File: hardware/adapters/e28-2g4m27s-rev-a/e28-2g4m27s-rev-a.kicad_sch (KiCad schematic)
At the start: 18 parts, among them J1 TSW-110-07-G-S, J2 TSW-108-07-G-S, U1 E28-2G4M27S, U2 AP63203WU-7

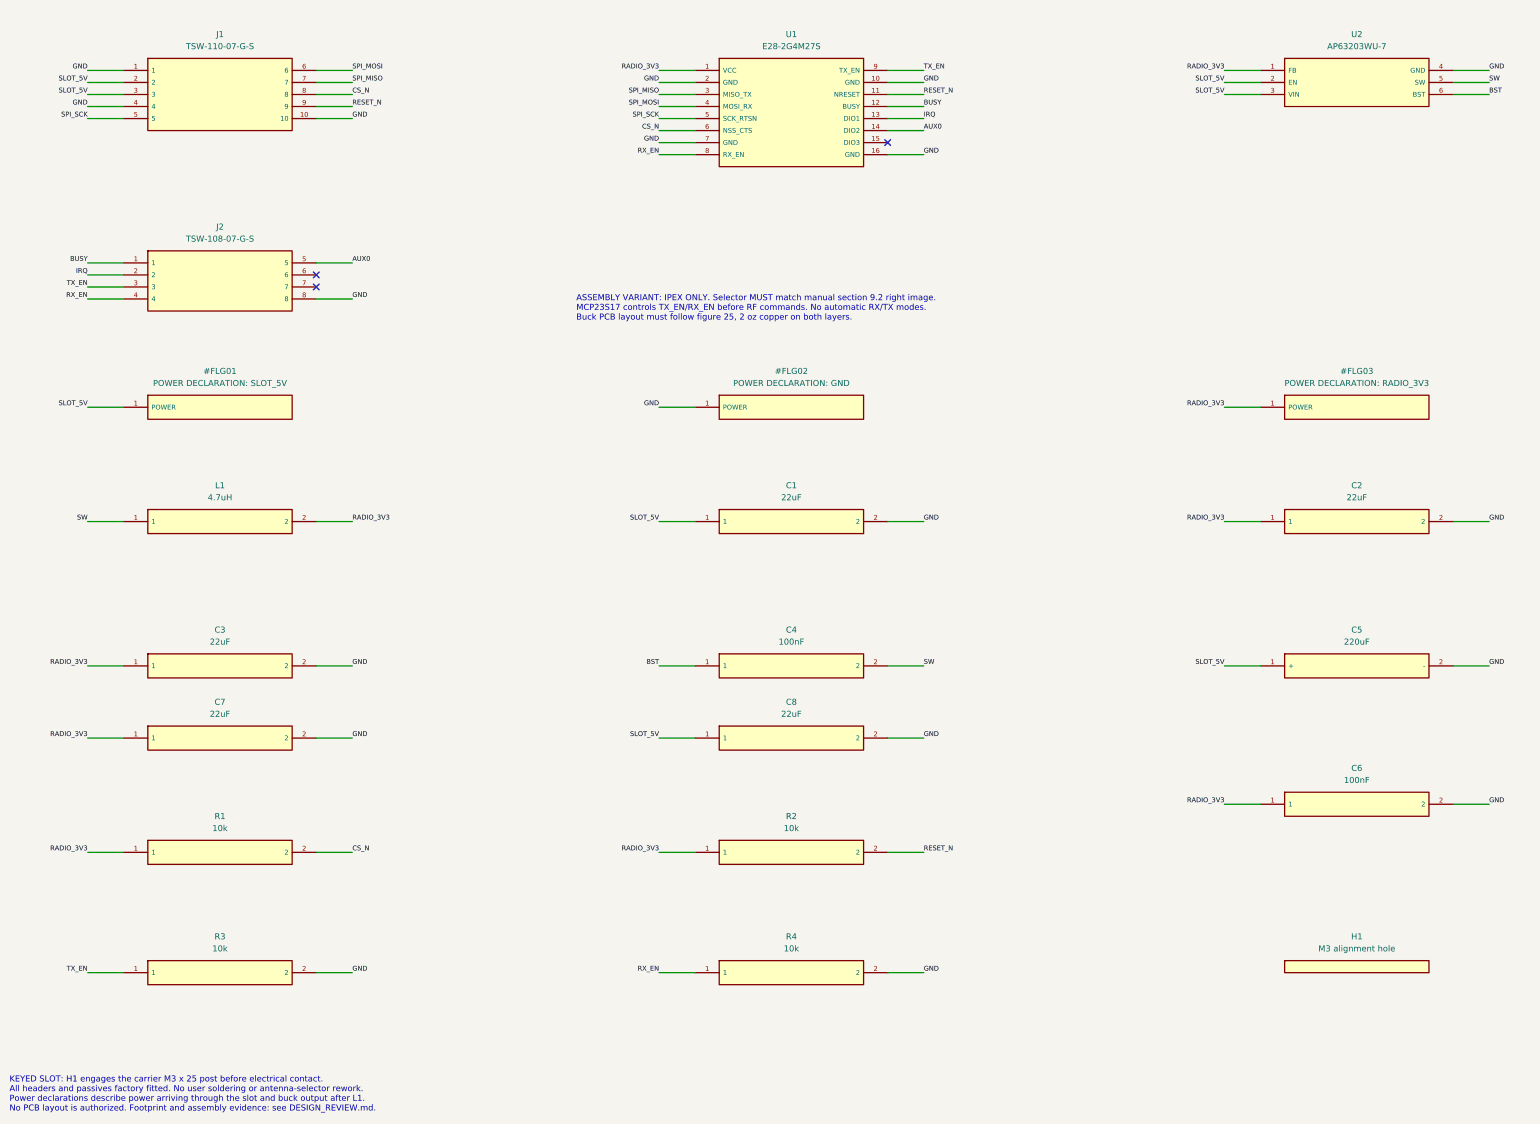
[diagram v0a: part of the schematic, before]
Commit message: Add configurable SPI source termination
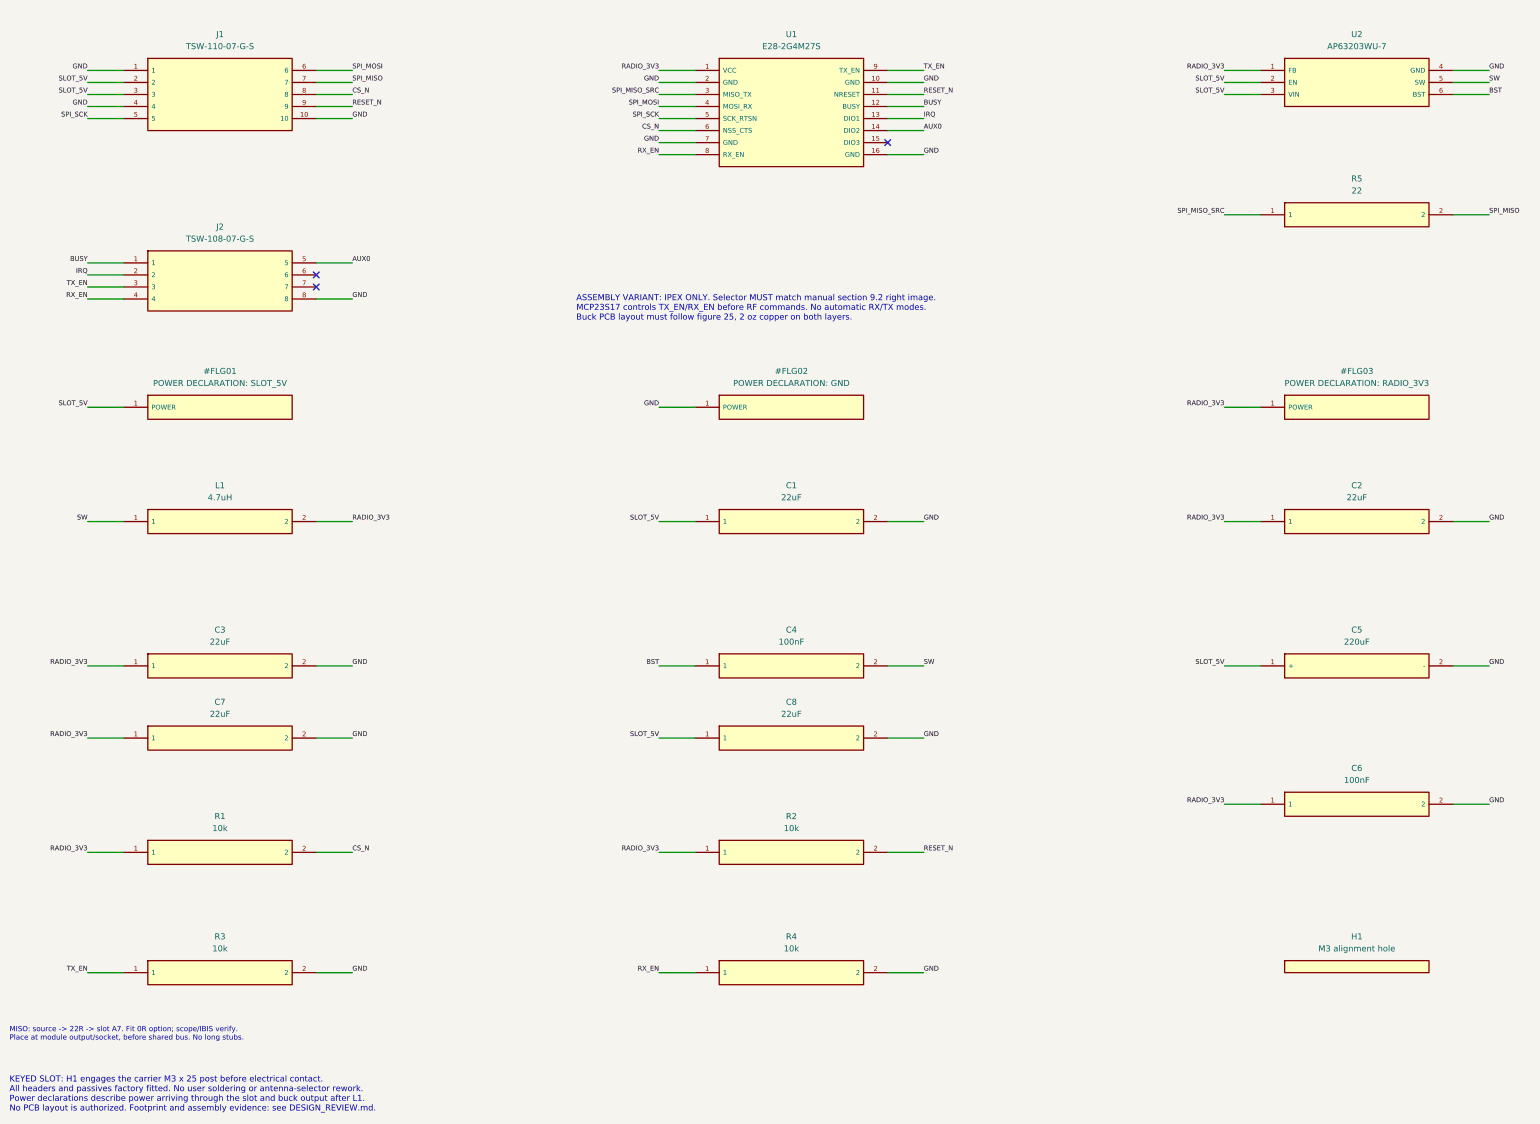
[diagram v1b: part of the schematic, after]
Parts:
- added R5: 22, Resistor_SMD:R_0603_1608Metric, symbol RadioLab:Resistor_value_only
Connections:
- net SPI_MISO: now also R5.2; no longer U1.3 (MISO_TX)
- new net SPI_MISO_SRC: R5.1, U1.3 (MISO_TX)
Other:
- note added: "MISO: source -> 22R -> slot A7. Fit 0R option; scope/IBIS verify. Place at module output/socket, before shared bus. No long stubs."

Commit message: Add routed Rev-A PCB layouts and board review
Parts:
- added TP1: SPI_SCK, RadioLab:Probe_Pad_D1.0mm, symbol RadioLab:Probe_point
- added TP10: IN_5V, RadioLab:Probe_Pad_D1.0mm, symbol RadioLab:Probe_point
- added TP11: CLIP_GND, TestPoint:TestPoint_Keystone_5010-5014_Multipurpose, symbol RadioLab:Probe_point
- added TP12: AUX0, RadioLab:Probe_Pad_D1.0mm, symbol RadioLab:Probe_point
- added TP13: OUT_3V3, RadioLab:Probe_Pad_D1.0mm, symbol RadioLab:Probe_point
- added TP14: REG_GND, RadioLab:Probe_Pad_D1.0mm, symbol RadioLab:Probe_point
- added TP15: EN_5V, RadioLab:Probe_Pad_D1.0mm, symbol RadioLab:Probe_point
- added TP16: SW, RadioLab:Probe_Pad_D0.6mm, symbol RadioLab:Probe_point
- added TP17: FB, RadioLab:Probe_Pad_D1.0mm, symbol RadioLab:Probe_point
- added TP18: MOD_3V3, RadioLab:Probe_Pad_D1.0mm, symbol RadioLab:Probe_point
- added TP19: MOD_GND, RadioLab:Probe_Pad_D1.0mm, symbol RadioLab:Probe_point
- added TP2: SPI_MOSI, RadioLab:Probe_Pad_D1.0mm, symbol RadioLab:Probe_point
- added TP20: SW_GND, RadioLab:Probe_Pad_D1.0mm, symbol RadioLab:Probe_point
- added TP3: SPI_MISO, RadioLab:Probe_Pad_D1.0mm, symbol RadioLab:Probe_point
- added TP4: CS_N, RadioLab:Probe_Pad_D1.0mm, symbol RadioLab:Probe_point
- added TP5: RESET_N, RadioLab:Probe_Pad_D1.0mm, symbol RadioLab:Probe_point
- added TP6: BUSY, RadioLab:Probe_Pad_D1.0mm, symbol RadioLab:Probe_point
- added TP7: IRQ, RadioLab:Probe_Pad_D1.0mm, symbol RadioLab:Probe_point
- added TP8: TX_EN, RadioLab:Probe_Pad_D1.0mm, symbol RadioLab:Probe_point
- added TP9: RX_EN, RadioLab:Probe_Pad_D1.0mm, symbol RadioLab:Probe_point
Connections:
- net AUX0: now also TP12.1 (PROBE)
- net BUSY: now also TP6.1 (PROBE)
- net CS_N: now also TP4.1 (PROBE)
- net GND: now also TP11.1 (PROBE), TP14.1 (PROBE), TP19.1 (PROBE), TP20.1 (PROBE)
- net IRQ: now also TP7.1 (PROBE)
- net RADIO_3V3: now also TP13.1 (PROBE), TP17.1 (PROBE), TP18.1 (PROBE)
- net RESET_N: now also TP5.1 (PROBE)
- net RX_EN: now also TP9.1 (PROBE)
- net SLOT_5V: now also TP10.1 (PROBE), TP15.1 (PROBE)
- net SPI_MISO: now also TP3.1 (PROBE)
- net SPI_MOSI: now also TP2.1 (PROBE)
- net SPI_SCK: now also TP1.1 (PROBE)
- net SW: now also TP16.1 (PROBE)
- net TX_EN: now also TP8.1 (PROBE)
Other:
- note added: "KEYED SLOT: H1 engages the carrier M3 x 25 post before electrical contact. All headers and passives factory fitted. No user soldering or antenna-selector rework. Power declarations describe power arriving through the slot and buck output after L1. Layout authorized; no fabrication release. See DESIGN_REVIEW.md."
- note added: "REV A LAYOUT REVIEW. NOT FOR FABRICATION."
- note removed: "KEYED SLOT: H1 engages the carrier M3 x 25 post before electrical contact. All headers and passives factory fitted. No user soldering or antenna-selector rework. Power declarations describe power arriving through the slot and buck output after L1. No PCB layout is authorized. Footprint and assembly evidence: see DESIGN_REVIEW.md."
- note removed: "REV A SCHEMATIC REVIEW. NO PCB LAYOUT OR FABRICATION RELEASE."
